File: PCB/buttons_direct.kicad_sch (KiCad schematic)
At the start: 3 parts

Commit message: refactor: erc is clean
This gets the schematic as clean as it can be.
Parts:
- removed SW_TRIG_DIG, SW_VOL_DN, SW_VOL_UP: Omron_B3F, symbol Switch:SW_Push
- added SW_TRIG_DIG1, SW_VOL_DN1, SW_VOL_UP1: Omron_B3F, symbol Switch:SW_Push
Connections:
- net BTN_TRIG_DIG: now also SW_TRIG_DIG1.1
- net BTN_VOL_DN: now also SW_VOL_DN1.1
- net BTN_VOL_UP: now also SW_VOL_UP1.1
- net GND: now also SW_TRIG_DIG1.2, SW_VOL_DN1.2, SW_VOL_UP1.2
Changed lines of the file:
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@@
+	(global_label "GND"
+		(shape passive)
+		(at 153.67 135.89 0)
+		(fields_autoplaced yes)
+		(effects
+			(font
+				(size 1.27 1.27)
+			)
+			(justify left)
+		)
+		(property "Intersheetrefs" "${INTERSHEET_REFS}"
+			(at 153.67 135.89 0)
+			(effects
+				(font
+					(size 1.27 1.27)
+				)
+				(hide yes)
+			)
+		)
+	)
 	(global_label "GND"
 		(shape passive)
@@
 		)
 	)
-	(global_label "GND"
-		(shape passive)
-		(at 153.67 135.89 0)
-		(fields_autoplaced yes)
-		(effects
-			(font
-				(size 1.27 1.27)
-			)
-			(justify left)
-		)
-		(property "Intersheetrefs" "${INTERSHEET_REFS}"
-			(at 153.67 135.89 0)
-			(effects
-				(font
-					(size 1.27 1.27)
-				)
-				(hide yes)
-			)
+	(hierarchical_label "BTN_VOL_UP"
+		(shape output)
+		(at 142.24 105.41 0)
+		(effects
+			(font
+				(size 1.27 1.27)
+			)
+			(justify left)
+		)
+	)
+	(hierarchical_label "BTN_TRIG_DIG"
+		(shape output)
+		(at 143.51 74.93 0)
+		(effects
+			(font
+				(size 1.27 1.27)
+			)
+			(justify left)
 		)
 	)
@@
 		)
 	)
-	(hierarchical_label "BTN_VOL_UP"
-		(shape output)
-		(at 142.24 105.41 0)
-		(effects
-			(font
-				(size 1.27 1.27)
-			)
-			(justify left)
-		)
-	)
-	(hierarchical_label "BTN_TRIG_DIG"
-		(shape output)
-		(at 143.51 74.93 0)
-		(effects
-			(font
-				(size 1.27 1.27)
-			)
-			(justify left)
+	(symbol
+		(lib_id "Switch:SW_Push")
+		(at 148.59 74.93 0)
+		(unit 1)
+		(exclude_from_sim no)
+		(in_bom yes)
+		(on_board yes)
+		(dnp no)
+		(fields_autoplaced yes)
+		(property "Reference" "SW_TRIG_DIG1"
+			(at 149.86 77.47 0)
+			(effects
+				(font
+					(size 1.27 1.27)
+				)
+				(justify left)
+			)
+		)
+		(property "Value" "Omron_B3F"
+			(at 148.59 73.406 0)
+			(effects
+				(font
+					(size 1.27 1.27)
+				)
+			)
+		)
+		(property "Footprint" ""
+			(at 148.59 80.01 0)
+			(effects
+				(font
+					(size 1.27 1.27)
+				)
+				(hide yes)
+			)
+		)
+		(property "Datasheet" "~"
+			(at 148.59 80.01 0)
+			(effects
+				(font
+					(size 1.27 1.27)
+				)
+				(hide yes)
+			)
+		)
+		(property "Description" "Push button switch, generic, two pins"
+			(at 148.59 74.93 0)
+			(effects
+				(font
+					(size 1.27 1.27)
+				)
+				(hide yes)
+			)
+		)
+		(pin "1"
+		)
+		(pin "2"
+		)
+		(instances
+			(project "snips_controller"
+				(path "/70589bdd-acbd-4920-8e78-aa58d10832b9/e2a172ff-869d-47d1-93b6-b7fd83cd5f36"
+					(reference "SW_TRIG_DIG1")
+					(unit 1)
+				)
+			)
+		)
+	)
+	(symbol
+		(lib_id "Switch:SW_Push")
+		(at 147.32 105.41 0)
+		(unit 1)
+		(exclude_from_sim no)
+		(in_bom yes)
+		(on_board yes)
+		(dnp no)
+		(fields_autoplaced yes)
+		(property "Reference" "SW_VOL_UP1"
+			(at 148.59 107.95 0)
+			(effects
+				(font
+					(size 1.27 1.27)
+				)
+				(justify left)
+			)
+		)
+		(property "Value" "Omron_B3F"
+			(at 147.32 103.886 0)
+			(effects
+				(font
+					(size 1.27 1.27)
+				)
+			)
+		)
+		(property "Footprint" ""
+			(at 147.32 110.49 0)
+			(effects
+				(font
+					(size 1.27 1.27)
+				)
+				(hide yes)
+			)
+		)
+		(property "Datasheet" "~"
+			(at 147.32 110.49 0)
+			(effects
+				(font
+					(size 1.27 1.27)
+				)
+				(hide yes)
+			)
+		)
+		(property "Description" "Push button switch, generic, two pins"
+			(at 147.32 105.41 0)
+			(effects
+				(font
+					(size 1.27 1.27)
+				)
+				(hide yes)
+			)
+		)
+		(pin "1"
+		)
+		(pin "2"
+		)
+		(instances
+			(project "snips_controller"
+				(path "/70589bdd-acbd-4920-8e78-aa58d10832b9/e2a172ff-869d-47d1-93b6-b7fd83cd5f36"
+					(reference "SW_VOL_UP1")
+					(unit 1)
+				)
+			)
 		)
 	)
@@
 		(dnp no)
 		(fields_autoplaced yes)
-		(property "Reference" "SW_VOL_DN"
+		(property "Reference" "SW_VOL_DN1"
 			(at 149.86 138.43 0)
 			(effects
@@
 		(instances
 			(project "snips_controller"
-				(path "/2289c08f-f540-4e27-86fd-a28b71d1d149/c01d6b19-237e-479b-ac5c-af6d5e4a0c9c"
-					(reference "SW_VOL_DN")
+				(path "/70589bdd-acbd-4920-8e78-aa58d10832b9/e2a172ff-869d-47d1-93b6-b7fd83cd5f36"
+					(reference "SW_VOL_DN1")
 					(unit 1)
 				)
-			)
-		)
-	)
-	(symbol
-		(lib_id "Switch:SW_Push")
-		(at 148.59 74.93 0)
-		(unit 1)
-		(exclude_from_sim no)
-		(in_bom yes)
-		(on_board yes)
-		(dnp no)
-		(fields_autoplaced yes)
-		(property "Reference" "SW_TRIG_DIG"
-			(at 149.86 77.47 0)
-			(effects
-				(font
-					(size 1.27 1.27)
-				)
-				(justify left)
-			)
-		)
-		(property "Value" "Omron_B3F"
-			(at 148.59 73.406 0)
-			(effects
-				(font
-					(size 1.27 1.27)
-				)
-			)
-		)
-		(property "Footprint" ""
-			(at 148.59 80.01 0)
-			(effects
-				(font
-					(size 1.27 1.27)
-				)
-				(hide yes)
-			)
-		)
-		(property "Datasheet" "~"
-			(at 148.59 80.01 0)
-			(effects
-				(font
-					(size 1.27 1.27)
-				)
-				(hide yes)
-			)
-		)
-		(property "Description" "Push button switch, generic, two pins"
-			(at 148.59 74.93 0)
-			(effects
-				(font
-					(size 1.27 1.27)
-				)
-				(hide yes)
-			)
-		)
-		(pin "1"
-		)
-		(pin "2"
-		)
-		(instances
-			(project "snips_controller"
-				(path "/2289c08f-f540-4e27-86fd-a28b71d1d149/c01d6b19-237e-479b-ac5c-af6d5e4a0c9c"
-					(reference "SW_TRIG_DIG")
-					(unit 1)
-				)
-			)
-		)
-	)
-	(symbol
-		(lib_id "Switch:SW_Push")
-		(at 147.32 105.41 0)
-		(unit 1)
-		(exclude_from_sim no)
-		(in_bom yes)
-		(on_board yes)
-		(dnp no)
-		(fields_autoplaced yes)
-		(property "Reference" "SW_VOL_UP"
-			(at 148.59 107.95 0)
-			(effects
-				(font
-					(size 1.27 1.27)
-				)
-				(justify left)
-			)
-		)
-		(property "Value" "Omron_B3F"
-			(at 147.32 103.886 0)
-			(effects
-				(font
-					(size 1.27 1.27)
-				)
-			)
-		)
-		(property "Footprint" ""
-			(at 147.32 110.49 0)
-			(effects
-				(font
-					(size 1.27 1.27)
-				)
-				(hide yes)
-			)
-		)
-		(property "Datasheet" "~"
-			(at 147.32 110.49 0)
-			(effects
-				(font
-					(size 1.27 1.27)
-				)
-				(hide yes)
-			)
-		)
-		(property "Description" "Push button switch, generic, two pins"
-			(at 147.32 105.41 0)
-			(effects
-				(font
-					(size 1.27 1.27)
-				)
-				(hide yes)
-			)
-		)
-		(pin "1"
-		)
-		(pin "2"
-		)
-		(instances
-			(project "snips_controller"
-				(path "/2289c08f-f540-4e27-86fd-a28b71d1d149/c01d6b19-237e-479b-ac5c-af6d5e4a0c9c"
-					(reference "SW_VOL_UP")
-					(unit 1)
-				)

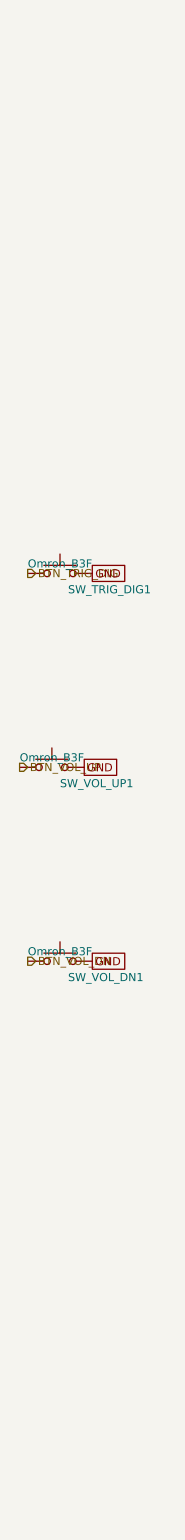
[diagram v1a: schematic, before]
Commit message: refactor: switch over to esp32-s3-wroom1 (#13)
This refactors to the esp32-s3 to avoid every problem we encountered with the raspberry pi options.
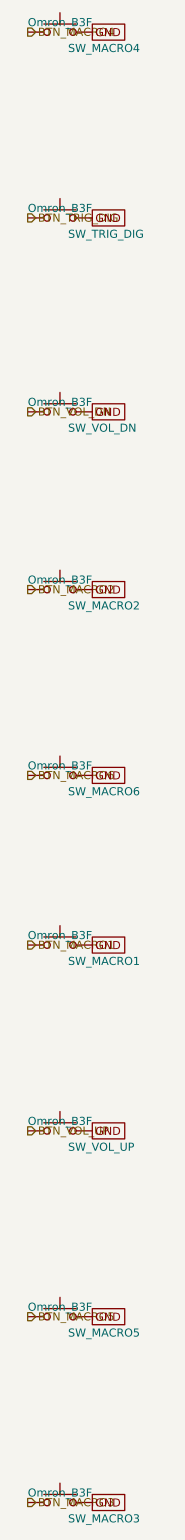
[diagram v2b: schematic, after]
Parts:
- removed SW_TRIG_DIG1, SW_VOL_DN1, SW_VOL_UP1: Omron_B3F, symbol Switch:SW_Push
- added SW_MACRO1, SW_MACRO2, SW_MACRO3, SW_MACRO4, SW_MACRO5, SW_MACRO6, SW_TRIG_DIG, SW_VOL_DN, SW_VOL_UP: Omron_B3F, Button_Switch_THT:SW_PUSH_6mm, symbol Switch:SW_Push
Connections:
- net BTN_TRIG_DIG: now also SW_TRIG_DIG.1
- net BTN_VOL_DN: now also SW_VOL_DN.1
- net BTN_VOL_UP: now also SW_VOL_UP.1
- net GND: now also SW_MACRO1.2, SW_MACRO2.2, SW_MACRO3.2, SW_MACRO4.2, SW_MACRO5.2, SW_MACRO6.2, SW_TRIG_DIG.2, SW_VOL_DN.2, SW_VOL_UP.2
- new net BTN_MACRO1: SW_MACRO1.1
- new net BTN_MACRO2: SW_MACRO2.1
- new net BTN_MACRO3: SW_MACRO3.1
- new net BTN_MACRO4: SW_MACRO4.1
- new net BTN_MACRO5: SW_MACRO5.1
- new net BTN_MACRO6: SW_MACRO6.1

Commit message: cleanup: annotations and library updates
This is just a task to update the kicad libraries and annotations internally to get that clean ERC.
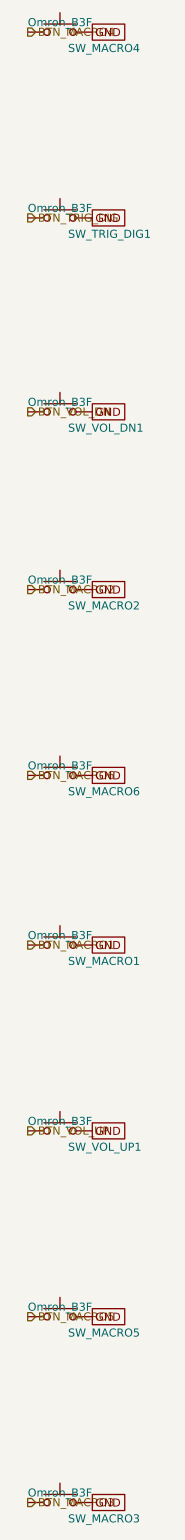
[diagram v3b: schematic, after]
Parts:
- renumbered SW_TRIG_DIG to SW_TRIG_DIG1, SW_VOL_DN to SW_VOL_DN1, SW_VOL_UP to SW_VOL_UP1
